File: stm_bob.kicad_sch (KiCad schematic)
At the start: 21 parts

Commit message: Version 1.1 - reworked all smd's to 0603
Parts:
- C10, C11, C12, C13, C4, C5, C6, C7, C8, C9: footprint Capacitor_SMD:C_0201_0603Metric_Pad0.64x0.40mm_HandSolder -> Capacitor_SMD:C_0603_1608Metric_Pad1.08x0.95mm_HandSolder
- R17: footprint Resistor_SMD:R_0201_0603Metric_Pad0.64x0.40mm_HandSolder -> Resistor_SMD:R_0603_1608Metric_Pad0.98x0.95mm_HandSolder
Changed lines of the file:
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@@
       (effects (font (size 1.27 1.27)))
     )
-    (property "Footprint" "Capacitor_SMD:C_0201_0603Metric_Pad0.64x0.40mm_HandSolder" (at 99.06 54.3052 0)
+    (property "Footprint" "Capacitor_SMD:C_0603_1608Metric_Pad1.08x0.95mm_HandSolder" (at 99.06 54.3052 0)
       (effects (font (size 1.27 1.27)) hide)
     )
@@
       (effects (font (size 1.27 1.27)))
     )
-    (property "Footprint" "Capacitor_SMD:C_0201_0603Metric_Pad0.64x0.40mm_HandSolder" (at 166.37 52.3748 0)
+    (property "Footprint" "Capacitor_SMD:C_0603_1608Metric_Pad1.08x0.95mm_HandSolder" (at 166.37 52.3748 0)
       (effects (font (size 1.27 1.27)) hide)
     )
@@
       (effects (font (size 1.27 1.27)))
     )
-    (property "Footprint" "Capacitor_SMD:C_0201_0603Metric_Pad0.64x0.40mm_HandSolder" (at 86.36 91.7448 0)
+    (property "Footprint" "Capacitor_SMD:C_0603_1608Metric_Pad1.08x0.95mm_HandSolder" (at 86.36 91.7448 0)
       (effects (font (size 1.27 1.27)) hide)
     )
@@
       (effects (font (size 1.27 1.27)))
     )
-    (property "Footprint" "Capacitor_SMD:C_0201_0603Metric_Pad0.64x0.40mm_HandSolder" (at 85.09 147.6248 0)
+    (property "Footprint" "Capacitor_SMD:C_0603_1608Metric_Pad1.08x0.95mm_HandSolder" (at 85.09 147.6248 0)
       (effects (font (size 1.27 1.27)) hide)
     )
@@
       (effects (font (size 1.27 1.27)))
     )
-    (property "Footprint" "Capacitor_SMD:C_0201_0603Metric_Pad0.64x0.40mm_HandSolder" (at 99.06 93.6752 0)
+    (property "Footprint" "Capacitor_SMD:C_0603_1608Metric_Pad1.08x0.95mm_HandSolder" (at 99.06 93.6752 0)
       (effects (font (size 1.27 1.27)) hide)
     )
@@
       (effects (font (size 1.27 1.27)) (justify left))
     )
-    (property "Footprint" "Resistor_SMD:R_0201_0603Metric_Pad0.64x0.40mm_HandSolder" (at 130.302 143.51 90)
+    (property "Footprint" "Resistor_SMD:R_0603_1608Metric_Pad0.98x0.95mm_HandSolder" (at 130.302 143.51 90)
       (effects (font (size 1.27 1.27)) hide)
     )
@@
       (effects (font (size 1.27 1.27)))
     )
-    (property "Footprint" "Capacitor_SMD:C_0201_0603Metric_Pad0.64x0.40mm_HandSolder" (at 17.78 149.5552 0)
+    (property "Footprint" "Capacitor_SMD:C_0603_1608Metric_Pad1.08x0.95mm_HandSolder" (at 17.78 149.5552 0)
       (effects (font (size 1.27 1.27)) hide)
     )
@@
       (effects (font (size 1.27 1.27)))
     )
-    (property "Footprint" "Capacitor_SMD:C_0201_0603Metric_Pad0.64x0.40mm_HandSolder" (at 86.36 53.6448 0)
+    (property "Footprint" "Capacitor_SMD:C_0603_1608Metric_Pad1.08x0.95mm_HandSolder" (at 86.36 53.6448 0)
       (effects (font (size 1.27 1.27)) hide)
     )
@@
       (effects (font (size 1.27 1.27)))
     )
-    (property "Footprint" "Capacitor_SMD:C_0201_0603Metric_Pad0.64x0.40mm_HandSolder" (at 19.05 93.6752 0)
+    (property "Footprint" "Capacitor_SMD:C_0603_1608Metric_Pad1.08x0.95mm_HandSolder" (at 19.05 93.6752 0)
       (effects (font (size 1.27 1.27)) hide)
     )
@@
       (effects (font (size 1.27 1.27)))
     )
-    (property "Footprint" "Capacitor_SMD:C_0201_0603Metric_Pad0.64x0.40mm_HandSolder" (at 19.05 55.5752 0)
+    (property "Footprint" "Capacitor_SMD:C_0603_1608Metric_Pad1.08x0.95mm_HandSolder" (at 19.05 55.5752 0)
       (effects (font (size 1.27 1.27)) hide)
     )
@@
       (effects (font (size 1.27 1.27)))
     )
-    (property "Footprint" "Capacitor_SMD:C_0201_0603Metric_Pad0.64x0.40mm_HandSolder" (at 166.37 90.4748 0)
-      (effects (font (size 1.27 1.27)) hide)
-    )
+    (property "Footprint" "Capacitor_SMD:C_0603_1608Metric_Pad1.08x0.95mm_HandSolder" (at 166.37 90.4748 0)
+      (effects (font (size 1.27 1.27)) hide)
+    )

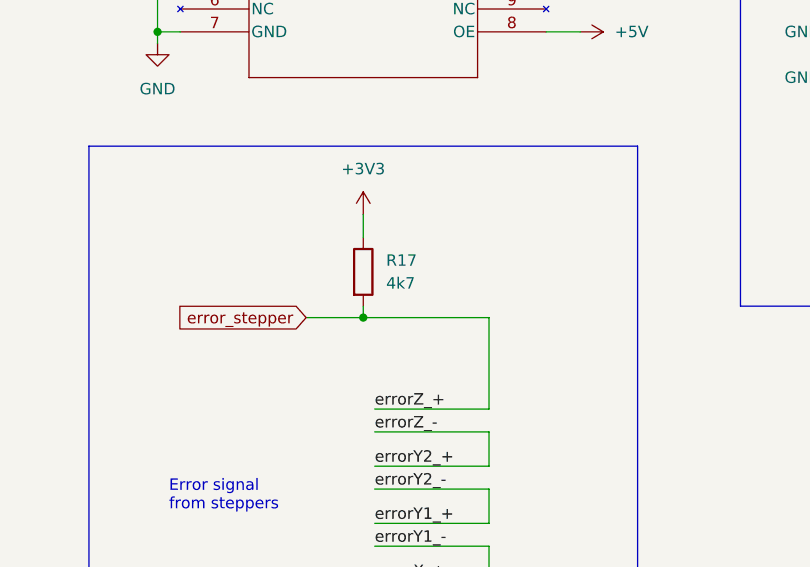
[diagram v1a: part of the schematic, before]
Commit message: Mainly value updates
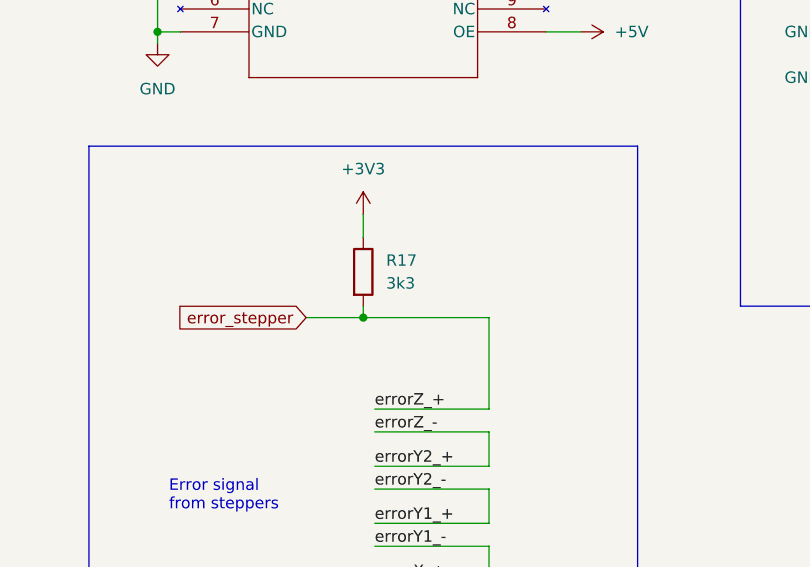
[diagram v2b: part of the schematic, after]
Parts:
- R17: value 4k7 -> 3k3
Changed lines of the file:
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@@
       (effects (font (size 1.27 1.27)) (justify left))
     )
-    (property "Value" "4k7" (at 134.62 144.78 0)
+    (property "Value" "3k3" (at 134.62 144.78 0)
       (effects (font (size 1.27 1.27)) (justify left))
     )
